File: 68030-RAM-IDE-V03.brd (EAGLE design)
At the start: 70 x 100 mm, 73 parts, among them IC1 REG1117, IC10 ICS570B, IC2 74HCT245PW, IC3 74AC16245, IC4 AM29F010S, IC5 74ALVT16543, IC6 74ALVT16543, IC7 XC95288XL-TQ144, IC8 K4S56163, IC9 K4S56163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

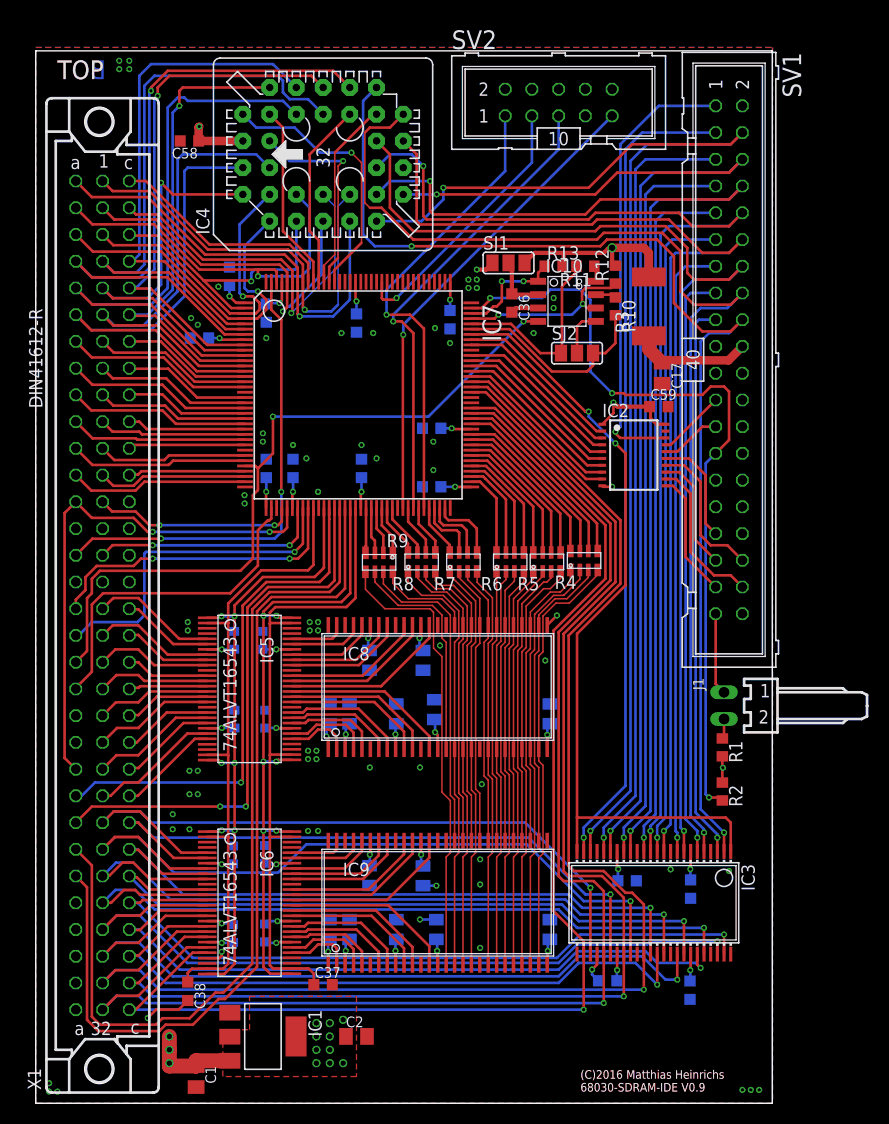
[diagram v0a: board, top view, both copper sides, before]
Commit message: Cleaned ARAM/BA signals
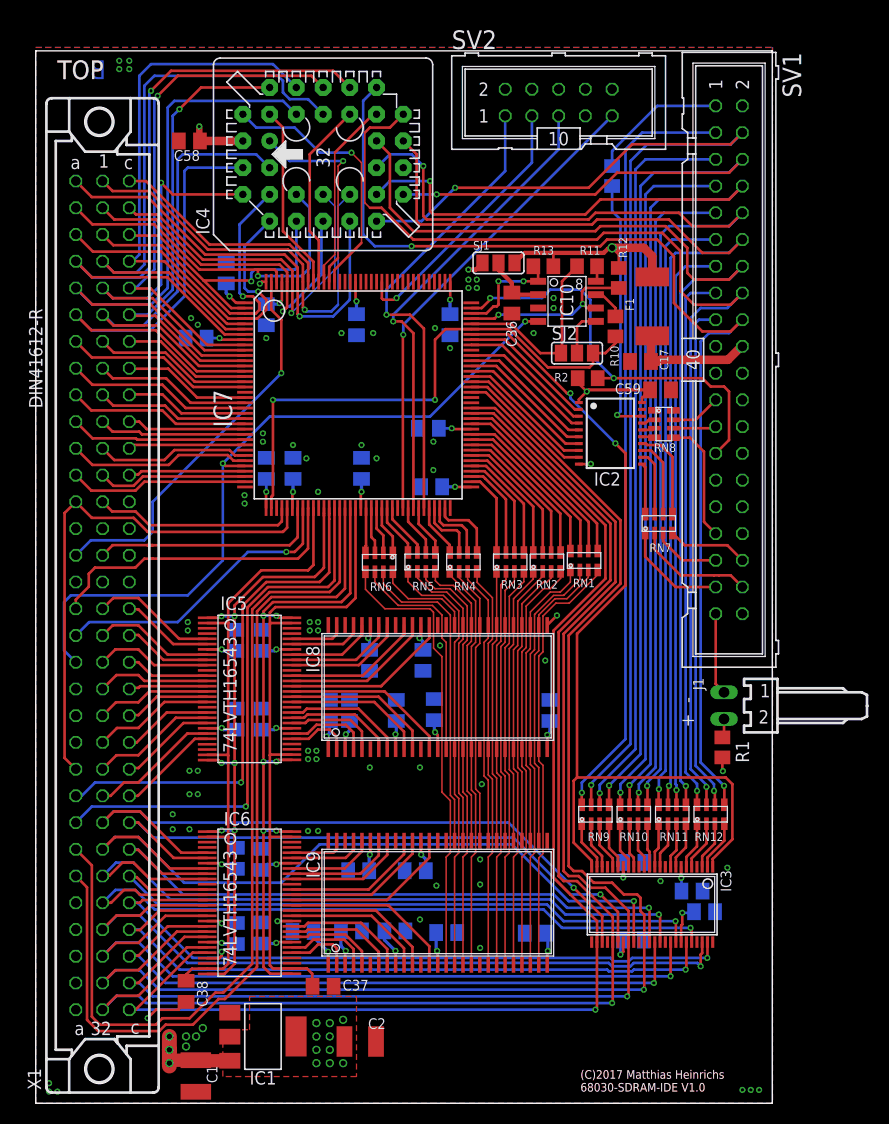
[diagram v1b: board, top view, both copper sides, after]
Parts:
- removed R3: 500mA, rcl:R2512
- added F1: 750mA, rcl:R2512
- added RN1, RN10, RN11, RN12, RN7, RN8, RN9: 22, SMD:R-NETZ@2
- C1, C2: value 47µF -> 22µF; device rcl:C0805K -> rcl:C1210K
- C10, C11, C12, C13, C14, C15, C16, C3, C4, C5, C6, C7, C8, C9: device SMD:0805 -> rcl:C0805K
- C17: value 47µF -> 10µF
- C18, C19, C20, C21, C22, C31, C32, C33, C34, C35, C37, C38, C58, C59, C60, C61, C62, C63: device rcl:C0603K -> rcl:C0805K
- C23, C24, C25, C26, C27, C28, C29, C30: value 10nF -> 100nF; device SMD:0603@3 -> rcl:C0805K
- C36: value (none) -> 100nF; device rcl:C0603K -> rcl:C0805K
- IC3: value 74AC16245 -> 74AC16245DGG; device 74ac-logic:SSOP48DL -> 74ac-logic:TSSOP48
- IC5, IC6: value 74ALVT16543 -> 74LVTH16543
- R1, R10, R11, R12, R13: device rcl:R0603 -> rcl:R0805
- R2: value 4.7 -> 4k7; device rcl:R0603 -> rcl:R0805
- R4: value 33R -> 22; device SMD:R-NETZ@2 -> rcl:R0805
- RN2, RN3, RN4, RN5, RN6: value 33R -> 22
- moved R2 41.3 mm to (52.5, 68.9), turned to 0 degrees
- moved R4 36.6 mm to (54.8, 88.1), flipped to the bottom, turned to 270 degrees
- moved C63 7.58 mm to (63.6, 18.2), turned to 180 degrees
- moved C62 4.57 mm to (56.8, 15.5), turned to 180 degrees
- moved IC2 3.03 mm to (54.6, 63.7)
- moved C16 2.52 mm to (25.4, 16.3), turned to 0 degrees
- moved C17 2.34 mm to (57.5, 70.5), turned to 180 degrees
- moved R10 1.91 mm to (55.1, 73.8)
- moved C60 1.86 mm to (56.8, 22.9)
- moved C59 1.60 mm to (59.4, 67.8)
- moved C11 1.44 mm to (47.5, 16.2), turned to 0 degrees
- moved C13 1.13 mm to (30.7, 22.1), turned to 0 degrees
- moved C14 1.02 mm to (39.1, 16.2), turned to 180 degrees
- moved R13 0.98 mm to (48.2, 79.5)
- moved SJ1 0.95 mm to (44.0, 79.9)
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- renumbered R5 to RN2, R6 to RN3, R7 to RN4, R8 to RN5, R9 to RN6
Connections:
- new net N$10: IC2.15, RN8.P$4
- new net N$11: IC2.18, R4.2
- new net N$12: IC2.17, RN8.P$2
- new net N$13: IC3.5, RN12.P$2
- new net N$14: IC3.6, RN12.P$1
- new net N$15: IC3.2, RN12.P$4
- new net N$16: IC3.3, RN12.P$3
- new net N$17: IC3.11, RN11.P$2
- new net N$18: IC3.12, RN11.P$1
- new net N$19: IC3.8, RN11.P$4
- new net N$2: IC2.12, RN7.P$7
- new net N$20: IC3.9, RN11.P$3
- new net N$21: IC3.16, RN10.P$2
- new net N$22: IC3.17, RN10.P$1
- new net N$23: IC3.13, RN10.P$4
- new net N$24: IC3.14, RN10.P$3
- new net N$27: IC3.22, RN9.P$2
- new net N$28: IC3.23, RN9.P$1
- new net N$29: IC3.19, RN9.P$4
- new net N$3: IC2.11, RN7.P$8
- new net N$30: IC3.20, RN9.P$3
- new net N$6: IC2.14, RN7.P$5
- new net N$7: IC2.13, RN7.P$6
- new net N$9: IC2.16, RN8.P$3
- net !IDE_R: now also RN8.P$6; no longer IC2.16
- net !IDE_W: now also RN8.P$7; no longer IC2.17
- net ARAM_2: now also RN1.P$2; no longer R4.P$2
- net ARAM_3: now also RN1.P$4; no longer R4.P$4
- net ARAM_4: now also RN1.P$3; no longer R4.P$3
- net ARAM_5: now also RN1.P$1; no longer R4.P$1
- net C_ARAM_2: now also RN1.P$7; no longer R4.P$7
- net C_ARAM_3: now also RN1.P$5; no longer R4.P$5
- net C_ARAM_4: now also RN1.P$6; no longer R4.P$6
- net C_ARAM_5: now also RN1.P$8; no longer R4.P$8
- net IDED0: now also RN12.P$6; no longer IC3.3
- net IDED1: now also RN12.P$8; no longer IC3.6
- net IDED10: now also RN10.P$7; no longer IC3.16
- net IDED11: now also RN10.P$5; no longer IC3.13
- net IDED12: now also RN11.P$7; no longer IC3.11
- net IDED13: now also RN11.P$5; no longer IC3.8
- net IDED14: now also RN12.P$7; no longer IC3.5
- net IDED15: now also RN12.P$5; no longer IC3.2
- net IDED2: now also RN11.P$6; no longer IC3.9
- net IDED3: now also RN11.P$8; no longer IC3.12
- net IDED4: now also RN10.P$6; no longer IC3.14
- net IDED5: now also RN10.P$8; no longer IC3.17
- net IDED6: now also RN9.P$6; no longer IC3.20
- net IDED7: now also RN9.P$8; no longer IC3.23
- net IDED8: now also RN9.P$7; no longer IC3.22
- net IDED9: now also RN9.P$5; no longer IC3.19
- net IDE_A0: now also RN7.P$3; no longer IC2.13
- net IDE_A1: now also RN8.P$5; no longer IC2.15
- net IDE_A2: now also RN7.P$4; no longer IC2.14
- net IDE_CS0: now also RN7.P$1; no longer IC2.11
- net IDE_CS1: now also RN7.P$2; no longer IC2.12
- net IDE_RST: now also R4.1; no longer IC2.18
- net IO_EXP: no longer IC7.38
- net KEY_PIN_POWER: now also F1.1; no longer R3.1
- net PLL_CLK_FULL: now also IC7.38
- net VCC: now also F1.2; no longer R3.2
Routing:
- net IDE_WAIT: track 75.0 -> 40.4 mm, vias 3 -> 2
- net PLL_CLK_FULL: track 19.8 -> 52.7 mm, vias 0 -> 2
- net IO_EXP: track 32.1 -> 0.00 mm
- net IDE_RST: track 43.2 -> 13.0 mm, vias 1 -> 0
- net N$11: track 0.00 -> 24.6 mm, vias 0 -> 1
- net GND: track 22.4 -> 12.1 mm, vias 74 -> 77
- net +3V3: track 88.3 -> 98.3 mm
- net N$6: track 0.00 -> 8.85 mm
- net C_IDE_BUFFER_DIR: track 76.9 -> 85.3 mm
- net N$7: track 0.00 -> 7.37 mm
- net !RESET: track 44.6 -> 37.4 mm, vias 2 -> 1
- net IDE_A2: track 14.0 -> 7.71 mm
- net N$2: track 0.00 -> 6.22 mm
- net IDED8: track 117.8 -> 112.7 mm
- net N$3: track 0.00 -> 4.87 mm
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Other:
- board text added: "(C)2017 Matthias Heinrichs 68030-SDRAM-IDE V1.0"
- board text added: "+ -"
- board text removed: "(C)2016 Matthias Heinrichs 68030-SDRAM-IDE V0.9"

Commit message: Updated the schematics for actual parts
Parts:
- IC7: value XC95288XL-TQ144 -> XC95144XL-TQ144
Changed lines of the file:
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@@
 <attribute name="VALUE" x="15.748" y="9.144" size="1.27" layer="27" ratio="10" rot="R270"/>
 </element>
-<element name="IC7" library="xilinx_xc9572xl-tq100" package="TQFP144" value="XC95288XL-TQ144" x="30.63875" y="67.31" smashed="yes" rot="R270">
+<element name="IC7" library="xilinx_xc9572xl-tq100" package="TQFP144" value="XC95144XL-TQ144" x="30.63875" y="67.31" smashed="yes" rot="R270">
 <attribute name="NAME" x="18.669" y="64.23025" size="1.778" layer="25" ratio="10" rot="R90"/>
 <attribute name="VALUE" x="28.09875" y="72.39" size="1.778" layer="27" ratio="10" rot="R270"/>

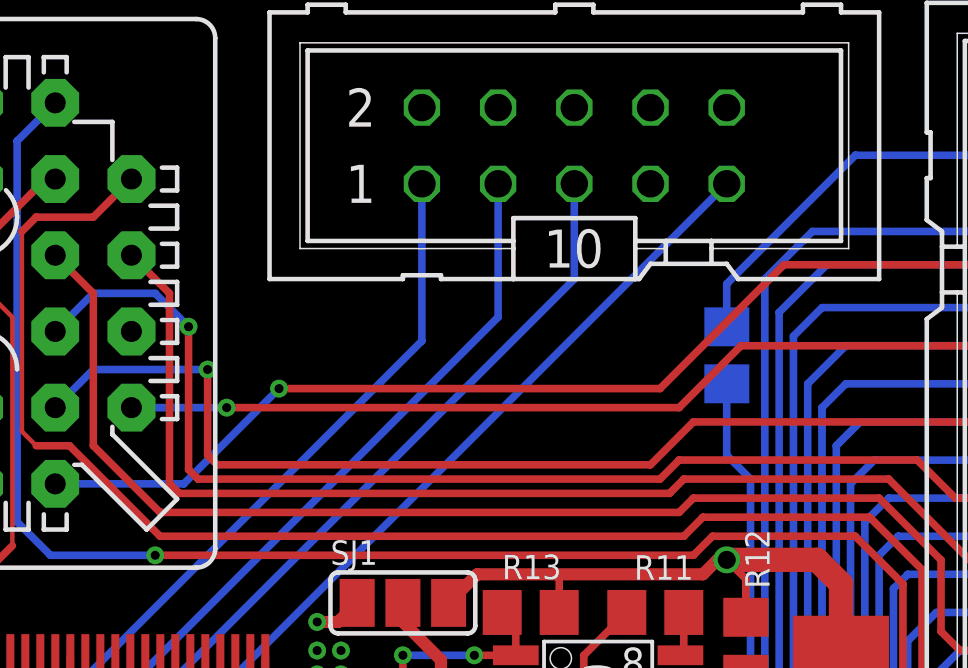
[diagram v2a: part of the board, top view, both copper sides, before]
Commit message: Added a JTAG-Pullup
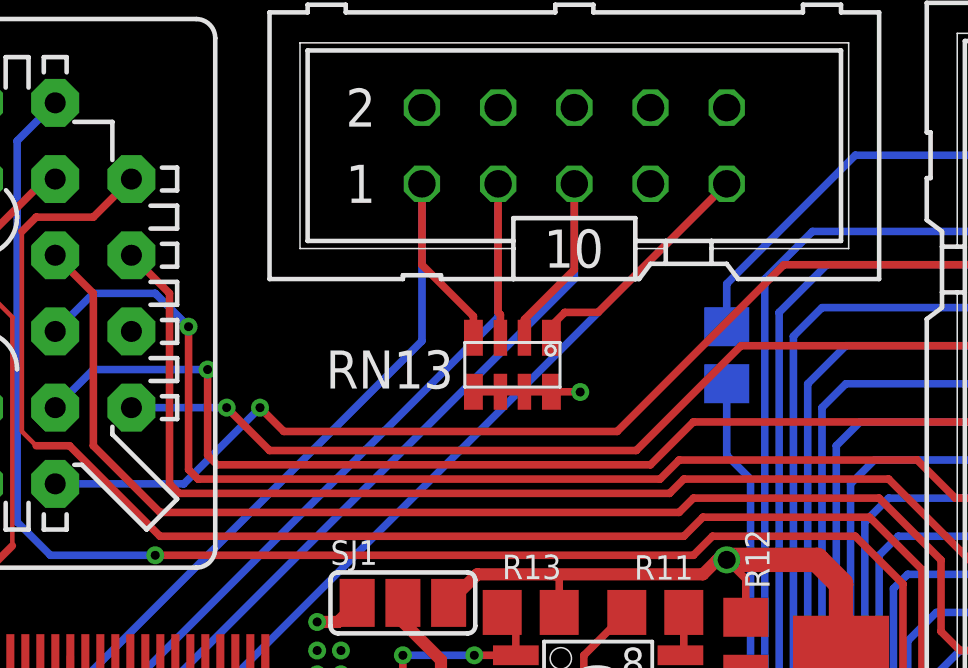
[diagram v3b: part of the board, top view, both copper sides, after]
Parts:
- added RN13: 4k7, SMD:R-NETZ@2
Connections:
- net TCK: now also RN13.P$4
- net TDI: now also RN13.P$1
- net TDO: now also RN13.P$3
- net TMS: now also RN13.P$2
- net VCC: now also RN13.P$5, RN13.P$6, RN13.P$7, RN13.P$8
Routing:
- net TDI: track 45.5 -> 53.7 mm
- net TCK: track 44.7 -> 50.5 mm
- net TMS: track 45.0 -> 50.9 mm
- net TDO: track 25.7 -> 30.9 mm
- net VCC: track 57.1 -> 60.7 mm, vias 11 -> 12
- net IDED9: track 104.4 -> 105.6 mm
- net IDED8: track 112.7 -> 113.4 mm
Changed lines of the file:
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@@
 </element>
 <element name="R4" library="rcl" package="R0805" value="22" x="54.76875" y="88.10625" rot="MR270"/>
+<element name="RN13" library="SMD" package="R-NETZ@2" value="4k7" x="47.625" y="87.78875" smashed="yes" rot="R180">
+<attribute name="NAME" x="45.6625" y="88.26625" size="1.27" layer="25" rot="R180"/>
+<attribute name="VALUE" x="51.125" y="86.38875" size="1.27" layer="27" rot="R180"/>
+</element>
 </elements>
 <signals>
@@
 <wire x1="15.2146" y1="4.0908" x2="12.9808" y2="4.0908" width="1.27" layer="1"/>
 <wire x1="12.9808" y1="4.0908" x2="12.7" y2="3.81" width="1.27" layer="1"/>
+<contactref element="RN13" pad="P$5"/>
+<contactref element="RN13" pad="P$6"/>
+<contactref element="RN13" pad="P$7"/>
+<contactref element="RN13" pad="P$8"/>
+<wire x1="46.325" y1="86.88875" x2="47.225" y2="86.88875" width="0.254" layer="1"/>
+<wire x1="47.225" y1="86.88875" x2="48.025" y2="86.88875" width="0.254" layer="1"/>
+<wire x1="48.025" y1="86.88875" x2="48.925" y2="86.88875" width="0.254" layer="1"/>
+<wire x1="48.925" y1="86.88875" x2="49.87755" y2="86.88875" width="0.254" layer="1"/>
+<wire x1="49.87755" y1="86.88875" x2="49.8856" y2="86.8807" width="0.254" layer="1"/>
+<via x="49.8856" y="86.8807" extent="1-16" drill="0.3"/>
 </signal>
 <signal name="GND">
@@
 <wire x1="25.88875" y1="56.56" x2="25.87625" y2="56.5475" width="0.254" layer="1"/>
 <wire x1="9.46785" y1="50.89525" x2="10.31875" y2="51.74615" width="0.254" layer="1"/>
-<wire x1="11.1125" y1="51.7525" x2="11.1125" y2="51.7525" width="0" layer="19" extent="1-16"/>
-<wire x1="24.13" y1="51.7525" x2="24.13" y2="51.7525" width="0" layer="19" extent="1-16"/>
-<wire x1="24.13" y1="51.7525" x2="24.92375" y2="51.7525" width="0" layer="19" extent="1-16"/>
 <wire x1="24.92375" y1="51.7525" x2="25.87625" y2="52.705" width="0.254" layer="1"/>
 <wire x1="25.87625" y1="52.705" x2="25.87625" y2="56.5475" width="0.254" layer="1"/>
@@
 <contactref element="IC4" pad="13"/>
 <wire x1="32.385" y1="83.82" x2="36.67125" y2="83.82" width="0.254" layer="16"/>
-<wire x1="36.67125" y1="83.82" x2="39.84625" y2="86.995" width="0.254" layer="16"/>
-<via x="39.84625" y="86.995" extent="1-16" drill="0.3"/>
-<wire x1="39.84625" y1="86.995" x2="52.54625" y2="86.995" width="0.254" layer="1"/>
-<wire x1="52.54625" y1="86.995" x2="56.67375" y2="91.1225" width="0.254" layer="1"/>
+<wire x1="36.67125" y1="83.82" x2="39.21125" y2="86.36" width="0.254" layer="16"/>
+<via x="39.21125" y="86.36" extent="1-16" drill="0.3"/>
+<wire x1="51.1175" y1="85.56625" x2="56.67375" y2="91.1225" width="0.254" layer="1"/>
 <wire x1="56.67375" y1="91.1225" x2="66.04" y2="91.1225" width="0.254" layer="1"/>
 <wire x1="66.04" y1="91.1225" x2="67.15125" y2="92.23375" width="0.254" layer="1"/>
@@
 <wire x1="52.78125" y1="28.36375" x2="52.78125" y2="30.23865" width="0.254" layer="1"/>
 <wire x1="52.78125" y1="30.23865" x2="52.7812" y2="30.2387" width="0.254" layer="1"/>
+<wire x1="51.1175" y1="85.56625" x2="40.005" y2="85.56625" width="0.254" layer="1"/>
+<wire x1="40.005" y1="85.56625" x2="39.21125" y2="86.36" width="0.254" layer="1"/>
 </signal>
 <signal name="IDED9">
@@
 <wire x1="34.925" y1="86.36" x2="38.1" y2="86.36" width="0.254" layer="16"/>
 <via x="38.1" y="86.36" extent="1-16" drill="0.3"/>
-<wire x1="38.1" y1="86.36" x2="53.18125" y2="86.36" width="0.254" layer="1"/>
-<wire x1="53.18125" y1="86.36" x2="55.245" y2="88.42375" width="0.254" layer="1"/>
+<wire x1="51.7525" y1="84.93125" x2="55.245" y2="88.42375" width="0.254" layer="1"/>
 <wire x1="55.245" y1="88.42375" x2="65.88125" y2="88.42375" width="0.254" layer="1"/>
 <wire x1="65.88125" y1="88.42375" x2="67.15125" y2="89.69375" width="0.254" layer="1"/>
@@
 <wire x1="54.48125" y1="28.36375" x2="54.48125" y2="30.1925" width="0.254" layer="1"/>
 <wire x1="54.48125" y1="30.1925" x2="54.483" y2="30.19425" width="0.254" layer="1"/>
+<wire x1="51.7525" y1="84.93125" x2="39.52875" y2="84.93125" width="0.254" layer="1"/>
+<wire x1="39.52875" y1="84.93125" x2="38.1" y2="86.36" width="0.254" layer="1"/>
 </signal>
 <signal name="IDED10">
@@
 <wire x1="34.925" y1="73.025" x2="34.925" y2="73.9775" width="0.254" layer="16"/>
 <wire x1="34.925" y1="73.9775" x2="54.76875" y2="93.82125" width="0.254" layer="16"/>
+<contactref element="RN13" pad="P$1"/>
+<wire x1="48.925" y1="88.68875" x2="48.925" y2="89.08875" width="0.254" layer="1"/>
+<wire x1="48.925" y1="89.08875" x2="49.37125" y2="89.535" width="0.254" layer="1"/>
+<wire x1="49.37125" y1="89.535" x2="50.4825" y2="89.535" width="0.254" layer="1"/>
+<wire x1="50.4825" y1="89.535" x2="54.76875" y2="93.82125" width="0.254" layer="1"/>
 </signal>
 <signal name="TDO">
@@
 <wire x1="34.29" y1="76.5175" x2="47.14875" y2="89.37625" width="0.254" layer="16"/>
 <wire x1="47.14875" y1="89.37625" x2="47.14875" y2="93.82125" width="0.254" layer="16"/>
+<contactref element="RN13" pad="P$3"/>
+<wire x1="47.225" y1="88.68875" x2="47.225" y2="89.45875" width="0.254" layer="1"/>
+<wire x1="47.225" y1="89.45875" x2="47.14875" y2="89.535" width="0.254" layer="1"/>
+<wire x1="47.14875" y1="89.535" x2="47.14875" y2="93.82125" width="0.254" layer="1"/>
 </signal>
 <signal name="TMS">
@@
 <wire x1="33.9725" y1="74.93" x2="49.68875" y2="90.64625" width="0.254" layer="16"/>
 <wire x1="49.68875" y1="90.64625" x2="49.68875" y2="93.82125" width="0.254" layer="16"/>
+<contactref element="RN13" pad="P$2"/>
+<wire x1="48.025" y1="88.68875" x2="48.025" y2="89.3" width="0.254" layer="1"/>
+<wire x1="48.025" y1="89.3" x2="49.68875" y2="90.96375" width="0.254" layer="1"/>
+<wire x1="49.68875" y1="90.96375" x2="49.68875" y2="93.82125" width="0.254" layer="1"/>
 </signal>
 <signal name="TCK">
@@
 <wire x1="33.3375" y1="77.31125" x2="44.60875" y2="88.5825" width="0.254" layer="16"/>
 <wire x1="44.60875" y1="88.5825" x2="44.60875" y2="93.82125" width="0.254" layer="16"/>
+<contactref element="RN13" pad="P$4"/>
+<wire x1="46.325" y1="88.68875" x2="46.325" y2="89.40625" width="0.254" layer="1"/>
+<wire x1="46.325" y1="89.40625" x2="44.60875" y2="91.1225" width="0.254" layer="1"/>
+<wire x1="44.60875" y1="91.1225" x2="44.60875" y2="93.82125" width="0.254" layer="1"/>
 </signal>
 <signal name="RAS">
